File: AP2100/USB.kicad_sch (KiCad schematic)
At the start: 28 parts

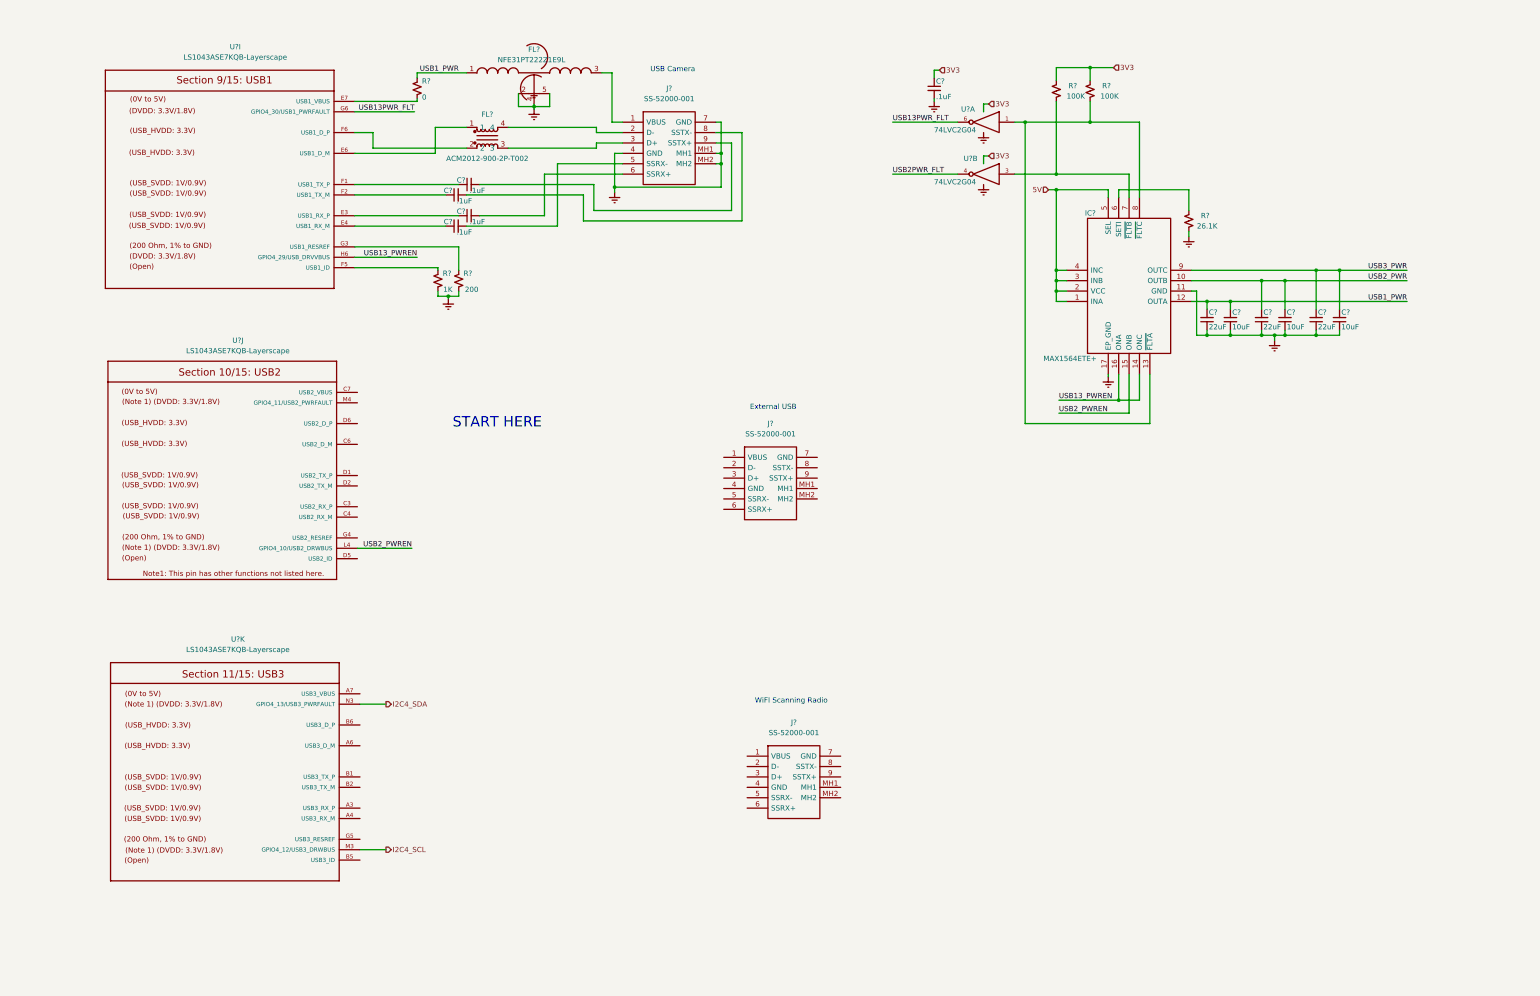
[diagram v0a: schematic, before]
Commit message: Annotate and update PCB with current design
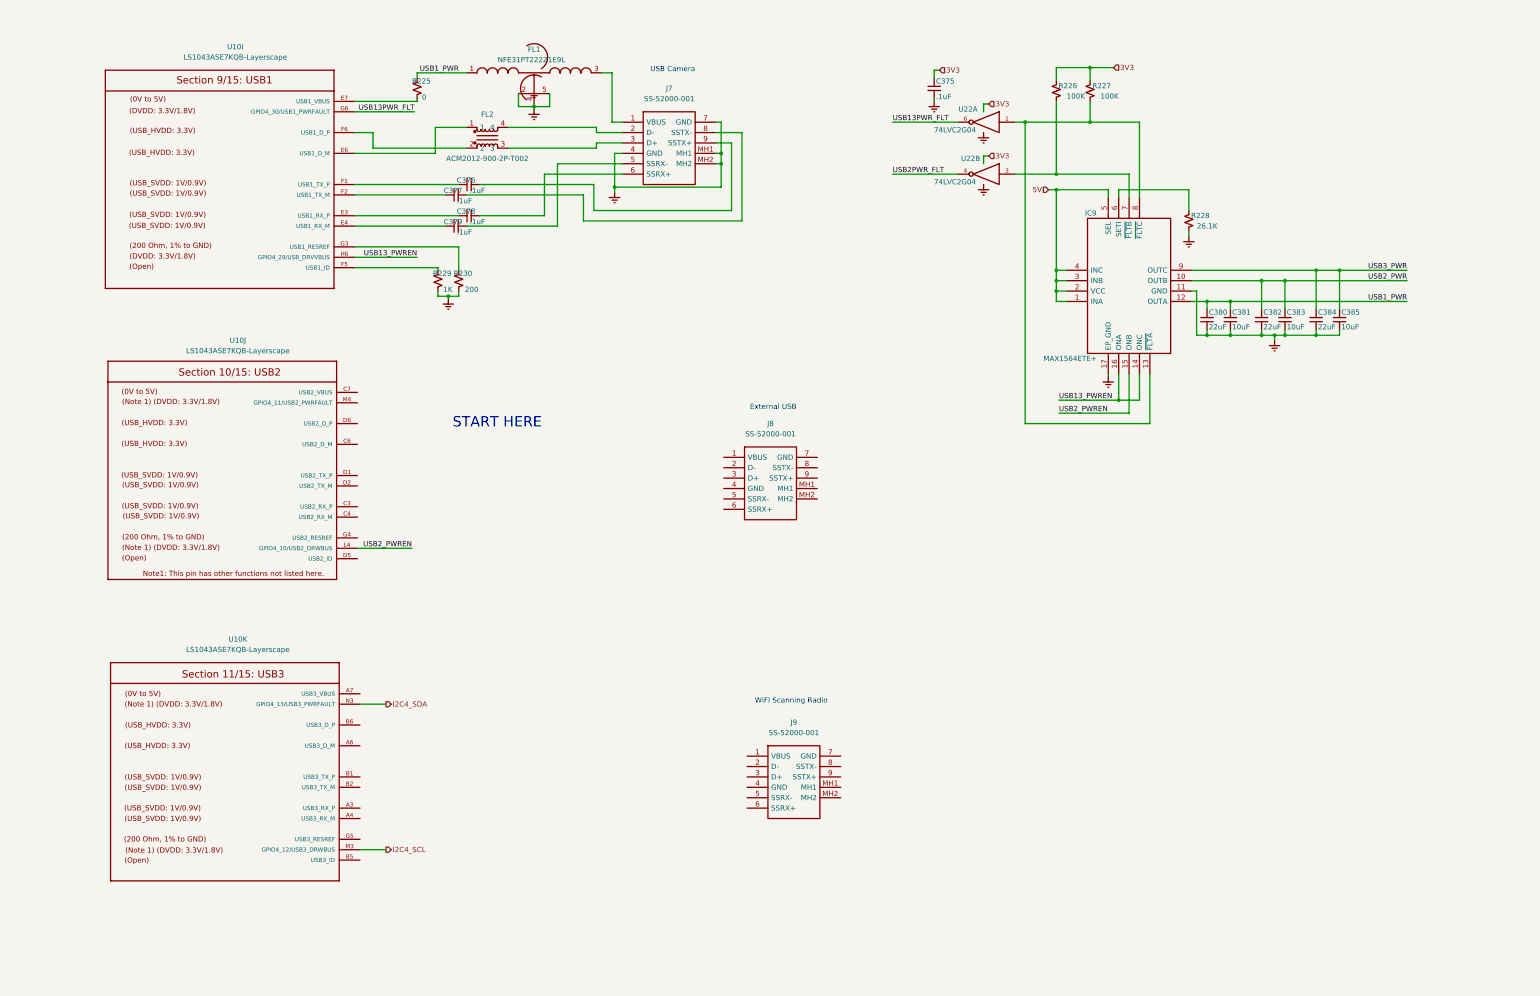
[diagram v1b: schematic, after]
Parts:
- gave numbers to parts that had none: 25

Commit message: RGMII ethernet section almost complete for 1st port Finish USB
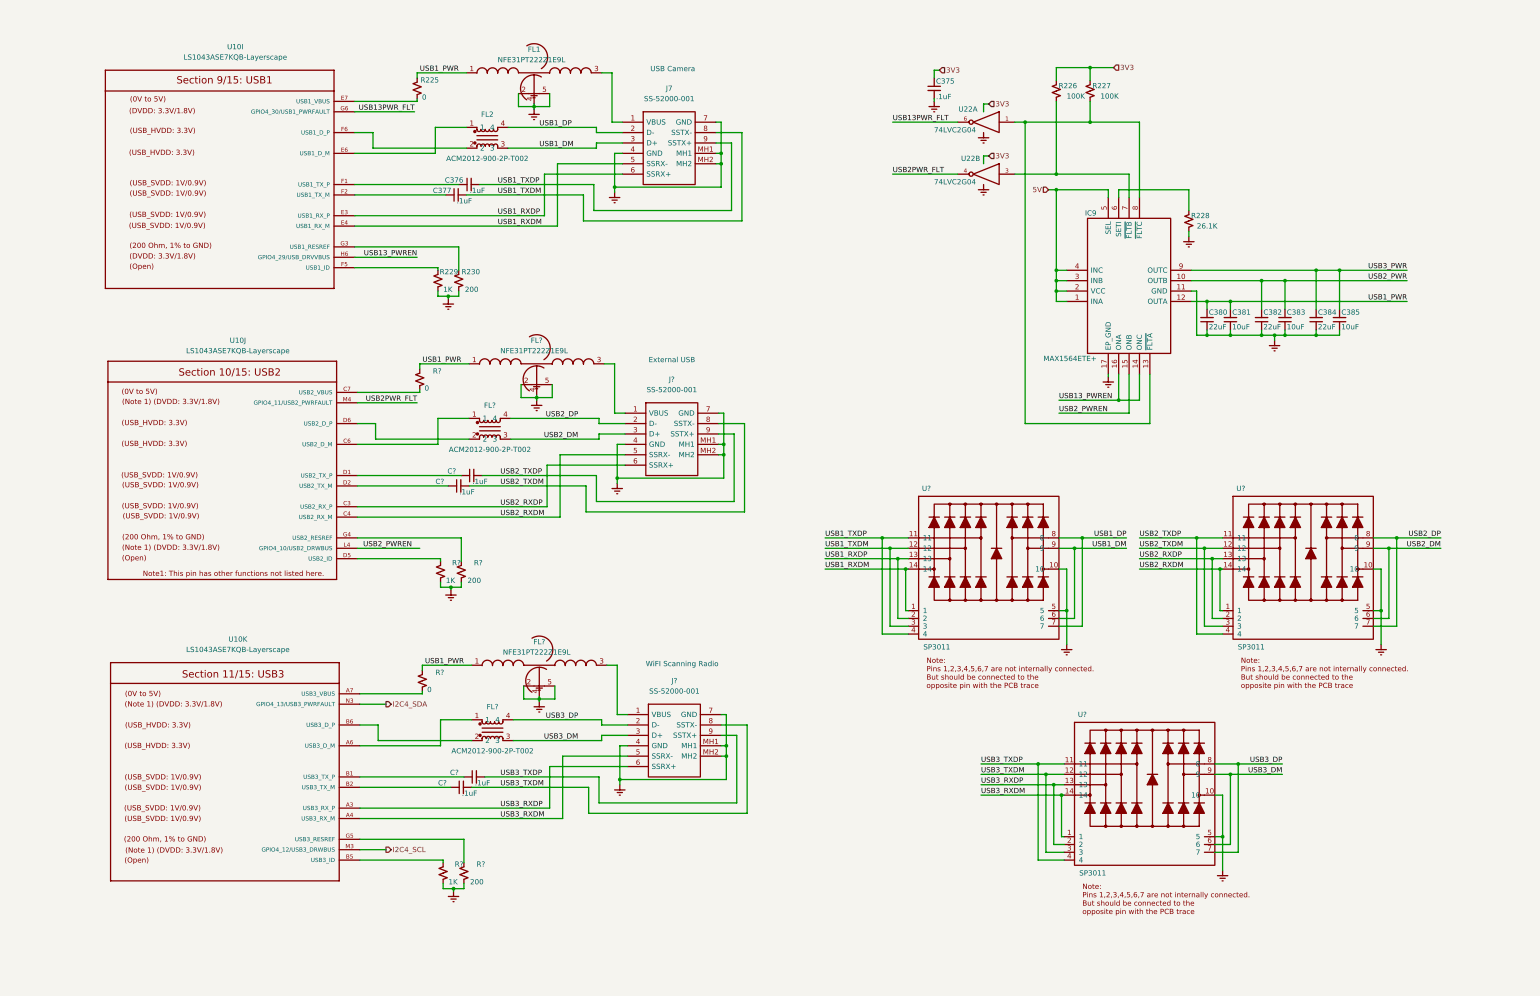
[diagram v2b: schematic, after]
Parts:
- removed C378, C379: .1uF, Capacitor_SMD:C_0402_1005Metric, symbol Device:C_Small
- removed J8, J9: SS-52000-001, SS52000001, symbol SS-52000-001:SS-52000-001
- added C? (x4): .1uF, Capacitor_SMD:C_0402_1005Metric, symbol Device:C_Small
- added FL? (x2): NFE31PT222Z1E9L, NFE31, symbol NFE31PT222Z1E9L:NFE31PT222Z1E9L
- added FL? (x2): ACM2012-900-2P-T002, ACM2012_1, symbol ACM2012-900-2P-T002:ACM2012-900-2P-T002
- added J? (x2): SS-52000-001, SS52000001, symbol SS-52000-001:SS-52000-001
- added R? (x2): 200, Resistor_SMD:R_0402_1005Metric, symbol Device:R_Small_US
- added R? (x2): 1K, Resistor_SMD:R_0402_1005Metric, symbol Device:R_Small_US
- added R? (x2): 0, Resistor_SMD:R_0402_1005Metric, symbol Device:R_Small_US
- added U? (x3): SP3011, Scott:uDFN-14_1.35x3.5mm_P0.5mm, symbol Scott:SP3011
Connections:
- net GND: now also FL?.2, FL?.2, FL?.4, FL?.4, FL?.5, FL?.5, J?.4 (GND), J?.4 (GND), J?.7 (GND), J?.7 (GND), J?.MH1, J?.MH1, J?.MH2, J?.MH2, R?.2, R?.2, R?.2, R?.2, U?.10, U?.10, U?.10, U?.5, U?.5, U?.5
- net USB1_PWR: now also FL?.1, FL?.1, R?.1, R?.1
- net USB2PWR_FLT: now also U10.M4 (GPIO4_11/USB2_PWRFAULT)
- net USB1_TXDP: now reaches C376.2, J7.9 (SSTX+)
- net USB1_TXDP: now also U?.11, U?.4
- net USB1_DM: now reaches FL2.3, J7.3 (D+)
- net USB1_DM: now also U?.6, U?.9
- net USB1_DP: now reaches FL2.4, J7.2 (D-)
- net USB1_DP: now also U?.7, U?.8
- net USB1_RXDP: now reaches U10.E3 (USB1_RX_P)
- net USB1_RXDP: now also J7.6 (SSRX+), U?.13, U?.2
- net USB1_RXDM: now reaches U10.E4 (USB1_RX_M)
- net USB1_RXDM: now also J7.5 (SSRX-), U?.1, U?.14
- net USB3_RXDP: now reaches U10.A3 (USB3_RX_P)
- net USB3_RXDP: now also J?.6 (SSRX+), U?.13, U?.2
- net USB3_RXDM: now reaches U10.A4 (USB3_RX_M)
- net USB3_RXDM: now also J?.5 (SSRX-), U?.1, U?.14
- net at U10.A6 (USB3_D_M): now also FL?.1
- net at U10.A7 (USB3_VBUS): now also R?.2
- net at U10.B1 (USB3_TX_P): now also C?.1
- net at U10.B2 (USB3_TX_M): now also C?.1
- net at U10.B5 (USB3_ID): now also R?.1
- net at U10.B6 (USB3_D_P): now also FL?.2
- net at U10.G5 (USB3_RESREF): now also R?.1
- net USB1_TXDM: now reaches C377.2, J7.8 (SSTX-)
- net USB1_TXDM: now also U?.12, U?.3
- net USB2_RXDP: now reaches U10.C3 (USB2_RX_P)
- net USB2_RXDP: now also J?.6 (SSRX+), U?.13, U?.2
- net USB2_RXDM: now reaches U10.C4 (USB2_RX_M)
- net USB2_RXDM: now also J?.5 (SSRX-), U?.1, U?.14
- net at U10.C6 (USB2_D_M): now also FL?.1
- net at U10.C7 (USB2_VBUS): now also R?.2
- net at U10.D1 (USB2_TX_P): now also C?.1
- net at U10.D2 (USB2_TX_M): now also C?.1
- net at U10.D5 (USB2_ID): now also R?.1
- net at U10.D6 (USB2_D_P): now also FL?.2
- net at U10.G4 (USB2_RESREF): now also R?.1
- new net: FL?.3, J?.1 (VBUS) (x2)
- new net USB2_DM: FL?.3, J?.3 (D+), U?.6, U?.9
- new net USB2_DP: FL?.4, J?.2 (D-), U?.7, U?.8
- new net USB2_TXDM: C?.2, J?.8 (SSTX-), U?.12, U?.3
- new net USB2_TXDP: C?.2, J?.9 (SSTX+), U?.11, U?.4
- new net USB3_DM: FL?.3, J?.3 (D+), U?.6, U?.9
- new net USB3_DP: FL?.4, J?.2 (D-), U?.7, U?.8
- new net USB3_TXDM: C?.2, J?.8 (SSTX-), U?.12, U?.3
- new net USB3_TXDP: C?.2, J?.9 (SSTX+), U?.11, U?.4
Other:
- note removed: "START HERE"

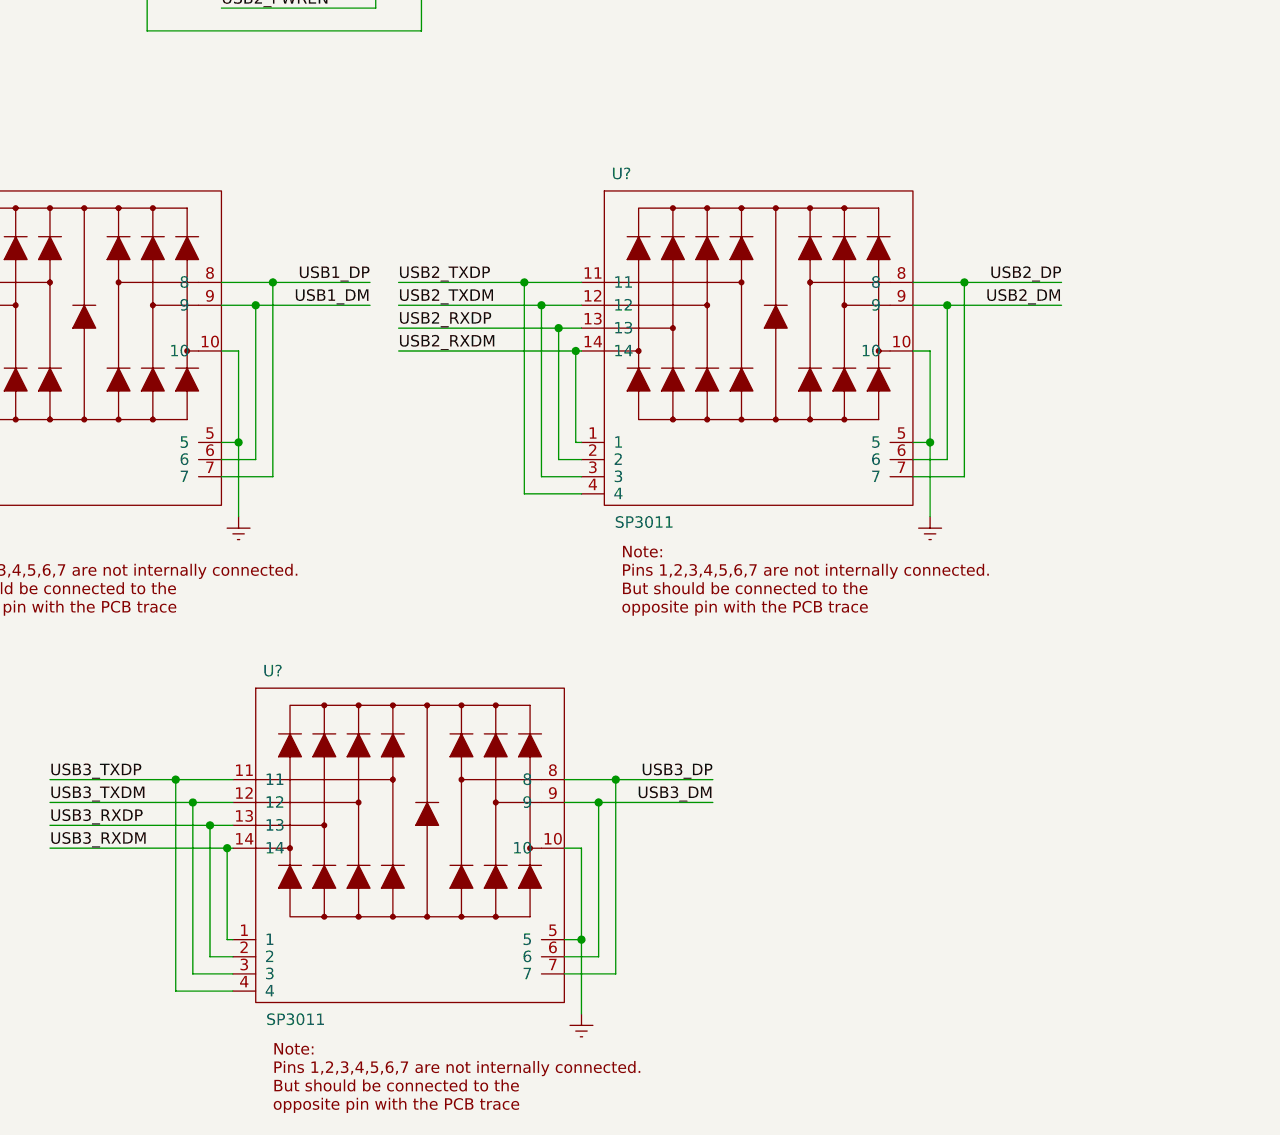
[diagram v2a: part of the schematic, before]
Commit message: Finish Ethernet all that's left is SerDes
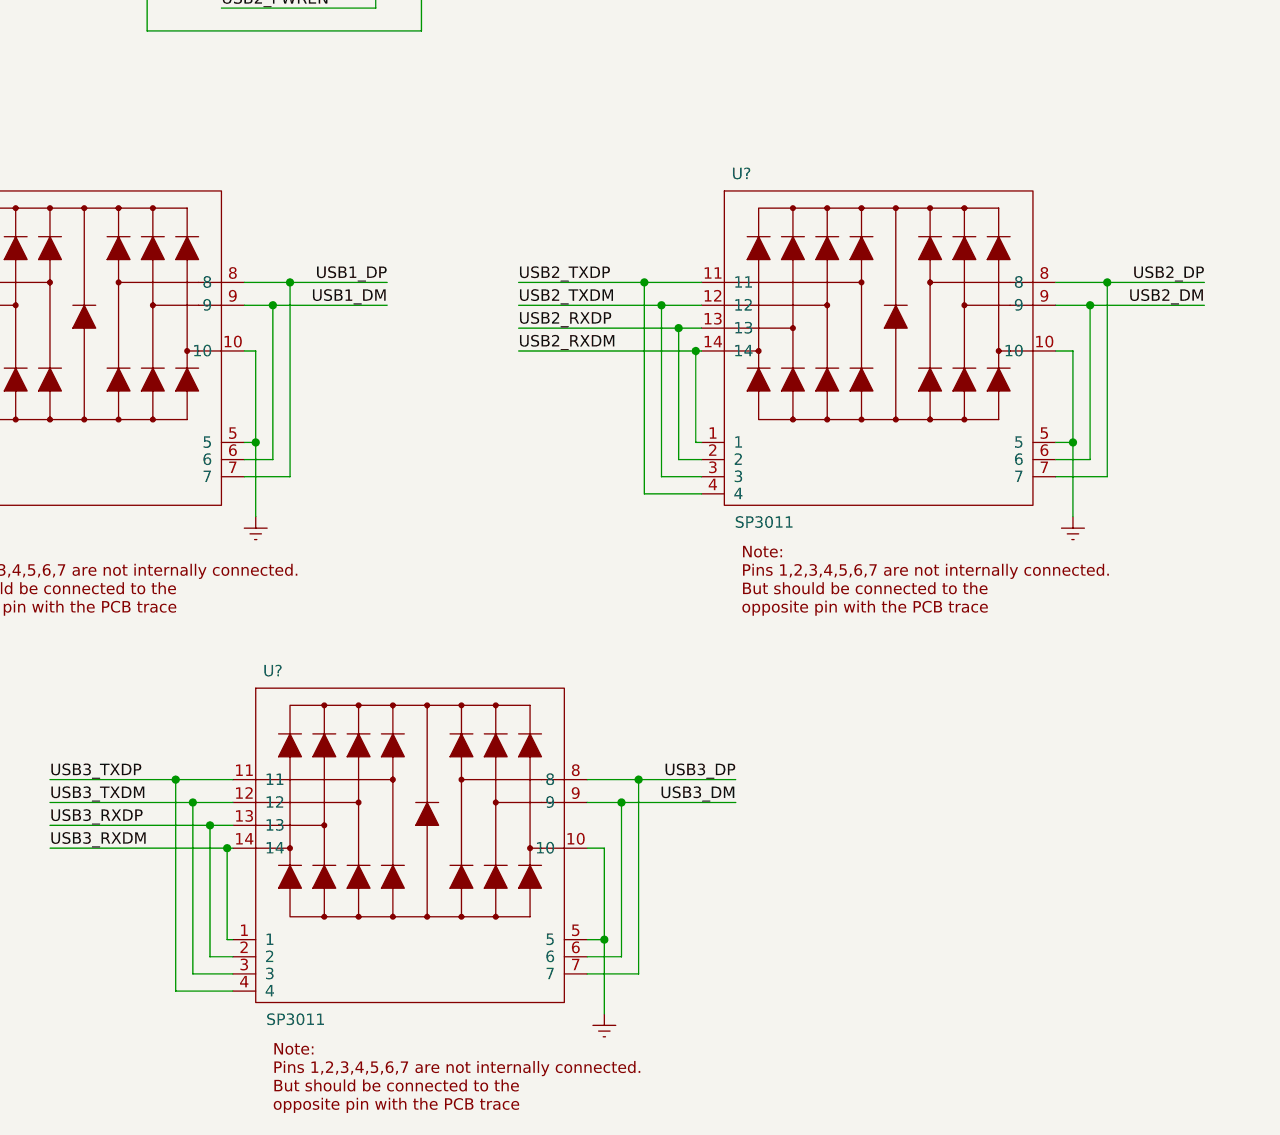
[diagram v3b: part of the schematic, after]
